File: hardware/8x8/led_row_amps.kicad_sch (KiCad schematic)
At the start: 10 parts

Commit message: Updated Pin Headers
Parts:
- renumbered Row_Amp_1 to Amp_1, Row_Amp_2 to Amp_2
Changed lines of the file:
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@@
   (symbol (lib_id "power:+5V") (at 220.98 95.25 0) (unit 1)
     (in_bom yes) (on_board yes)
-    (property "Reference" "#PWR04" (id 0) (at 220.98 99.06 0)
+    (property "Reference" "#PWR0103" (id 0) (at 220.98 99.06 0)
       (effects (font (size 1.27 1.27)) hide)
     )
@@
   (symbol (lib_id "power:+9V") (at 93.98 64.77 0) (unit 1)
     (in_bom yes) (on_board yes)
-    (property "Reference" "#PWR01" (id 0) (at 93.98 68.58 0)
+    (property "Reference" "#PWR0101" (id 0) (at 93.98 68.58 0)
       (effects (font (size 1.27 1.27)) hide)
     )
@@
   (symbol (lib_id "power:+5V") (at 93.98 95.25 0) (unit 1)
     (in_bom yes) (on_board yes)
-    (property "Reference" "#PWR02" (id 0) (at 93.98 99.06 0)
+    (property "Reference" "#PWR0102" (id 0) (at 93.98 99.06 0)
       (effects (font (size 1.27 1.27)) hide)
     )
@@
   (symbol (lib_id "Op-Amp:MCP619-I{brace}slash}SL") (at 76.2 81.28 0) (unit 1)
     (in_bom yes) (on_board yes) (fields_autoplaced)
-    (property "Reference" "Row_Amp_1" (id 0) (at 76.2 60.96 0))
+    (property "Reference" "Amp_1" (id 0) (at 76.2 60.96 0))
     (property "Value" "MCP619-I{slash}SL" (id 1) (at 76.2 60.96 0)
       (effects (font (size 1.27 1.27)) hide)
@@
   (symbol (lib_id "Op-Amp:MCP619-I{brace}slash}SL") (at 203.2 81.28 0) (unit 1)
     (in_bom yes) (on_board yes) (fields_autoplaced)
-    (property "Reference" "Row_Amp_2" (id 0) (at 203.2 60.96 0))
+    (property "Reference" "Amp_2" (id 0) (at 203.2 60.96 0))
     (property "Value" "MCP619-I{slash}SL" (id 1) (at 203.2 60.96 0)
       (effects (font (size 1.27 1.27)) hide)
@@
   (symbol (lib_id "power:+9V") (at 220.98 64.77 0) (unit 1)
     (in_bom yes) (on_board yes)
-    (property "Reference" "#PWR03" (id 0) (at 220.98 68.58 0)
+    (property "Reference" "#PWR0104" (id 0) (at 220.98 68.58 0)
       (effects (font (size 1.27 1.27)) hide)
     )

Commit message: Temporary Component Placement on PCB
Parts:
- renumbered Amp_1 to AMP_1, Amp_2 to AMP_2
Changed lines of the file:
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@@
   (symbol (lib_id "Op-Amp:MCP619-I{brace}slash}SL") (at 76.2 81.28 0) (unit 1)
     (in_bom yes) (on_board yes) (fields_autoplaced)
-    (property "Reference" "Amp_1" (id 0) (at 76.2 60.96 0))
+    (property "Reference" "AMP_1" (id 0) (at 76.2 60.96 0))
     (property "Value" "MCP619-I{slash}SL" (id 1) (at 76.2 60.96 0)
       (effects (font (size 1.27 1.27)) hide)
@@
   (symbol (lib_id "Op-Amp:MCP619-I{brace}slash}SL") (at 203.2 81.28 0) (unit 1)
     (in_bom yes) (on_board yes) (fields_autoplaced)
-    (property "Reference" "Amp_2" (id 0) (at 203.2 60.96 0))
+    (property "Reference" "AMP_2" (id 0) (at 203.2 60.96 0))
     (property "Value" "MCP619-I{slash}SL" (id 1) (at 203.2 60.96 0)
       (effects (font (size 1.27 1.27)) hide)

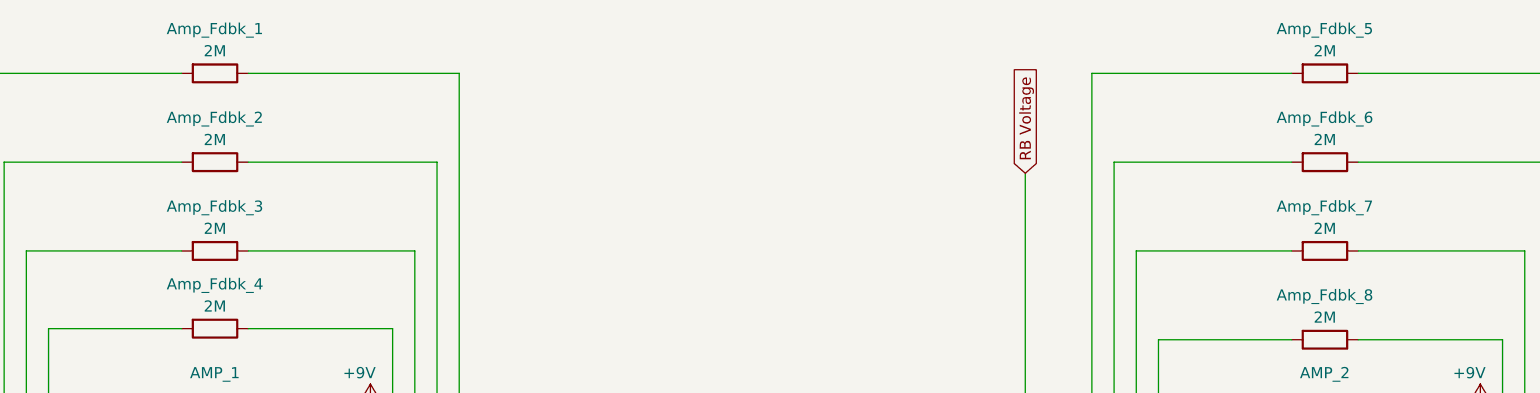
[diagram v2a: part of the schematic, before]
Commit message: Rearranged PCB Components
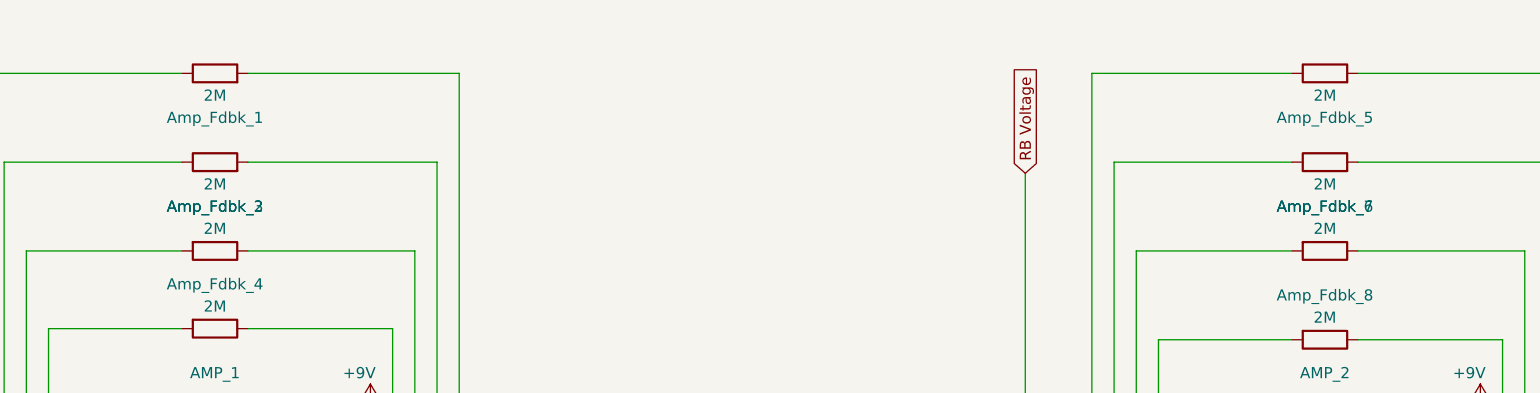
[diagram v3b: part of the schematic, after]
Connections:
- net Amp_IP_1: now also Amp_Fdbk_1.1; no longer Amp_Fdbk_1.2
- net Amp_IP_2: now also Amp_Fdbk_2.1; no longer Amp_Fdbk_2.2
- net Amp_IP_5: now also Amp_Fdbk_5.1; no longer Amp_Fdbk_5.2
- net Amp_IP_6: now also Amp_Fdbk_6.1; no longer Amp_Fdbk_6.2
- net Amp_OP_1: now also Amp_Fdbk_1.2; no longer Amp_Fdbk_1.1
- net Amp_OP_2: now also Amp_Fdbk_2.2; no longer Amp_Fdbk_2.1
- net Amp_OP_5: now also Amp_Fdbk_5.2; no longer Amp_Fdbk_5.1
- net Amp_OP_6: now also Amp_Fdbk_6.2; no longer Amp_Fdbk_6.1
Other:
- moved on the sheet: Amp_Fdbk_1, Amp_Fdbk_2, Amp_Fdbk_5, Amp_Fdbk_6
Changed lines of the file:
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@@
     (effects (font (size 1.27 1.27)) (justify left))
   )
-  (symbol (lib_id "Device:R") (at 76.2 36.83 270) (unit 1)
+  (symbol (lib_id "Device:R") (at 76.2 36.83 90) (unit 1)
     (in_bom yes) (on_board yes)
-    (property "Reference" "Amp_Fdbk_2" (id 0) (at 76.2 31.75 90))
-    (property "Value" "2M" (id 1) (at 76.2 34.29 90))
-    (property "Footprint" "Resistor_THT:R_Axial_DIN0207_L6.3mm_D2.5mm_P7.62mm_Horizontal" (id 2) (at 76.2 35.052 90)
+    (property "Reference" "Amp_Fdbk_2" (id 0) (at 76.2 41.91 90))
+    (property "Value" "2M" (id 1) (at 76.2 39.37 90))
+    (property "Footprint" "Resistor_THT:R_Axial_DIN0207_L6.3mm_D2.5mm_P7.62mm_Horizontal" (id 2) (at 76.2 38.608 90)
       (effects (font (size 1.27 1.27)) hide)
     )
@@
     (pin "2")
   )
-  (symbol (lib_id "Device:R") (at 203.2 36.83 270) (unit 1)
+  (symbol (lib_id "Device:R") (at 203.2 36.83 90) (unit 1)
     (in_bom yes) (on_board yes)
-    (property "Reference" "Amp_Fdbk_6" (id 0) (at 203.2 31.75 90))
-    (property "Value" "2M" (id 1) (at 203.2 34.29 90))
-    (property "Footprint" "Resistor_THT:R_Axial_DIN0207_L6.3mm_D2.5mm_P7.62mm_Horizontal" (id 2) (at 203.2 35.052 90)
+    (property "Reference" "Amp_Fdbk_6" (id 0) (at 203.2 41.91 90))
+    (property "Value" "2M" (id 1) (at 203.2 39.37 90))
+    (property "Footprint" "Resistor_THT:R_Axial_DIN0207_L6.3mm_D2.5mm_P7.62mm_Horizontal" (id 2) (at 203.2 38.608 90)
       (effects (font (size 1.27 1.27)) hide)
     )
@@
     (pin "1")
   )
-  (symbol (lib_id "Device:R") (at 203.2 26.67 270) (unit 1)
+  (symbol (lib_id "Device:R") (at 203.2 26.67 90) (unit 1)
     (in_bom yes) (on_board yes)
-    (property "Reference" "Amp_Fdbk_5" (id 0) (at 203.2 21.59 90))
-    (property "Value" "2M" (id 1) (at 203.2 24.13 90))
-    (property "Footprint" "Resistor_THT:R_Axial_DIN0207_L6.3mm_D2.5mm_P7.62mm_Horizontal" (id 2) (at 203.2 24.892 90)
+    (property "Reference" "Amp_Fdbk_5" (id 0) (at 203.2 31.75 90))
+    (property "Value" "2M" (id 1) (at 203.2 29.21 90))
+    (property "Footprint" "Resistor_THT:R_Axial_DIN0207_L6.3mm_D2.5mm_P7.62mm_Horizontal" (id 2) (at 203.2 28.448 90)
       (effects (font (size 1.27 1.27)) hide)
     )
@@
     (pin "2")
   )
-  (symbol (lib_id "Device:R") (at 76.2 26.67 270) (unit 1)
+  (symbol (lib_id "Device:R") (at 76.2 26.67 90) (unit 1)
     (in_bom yes) (on_board yes)
-    (property "Reference" "Amp_Fdbk_1" (id 0) (at 76.2 21.59 90))
-    (property "Value" "2M" (id 1) (at 76.2 24.13 90))
-    (property "Footprint" "Resistor_THT:R_Axial_DIN0207_L6.3mm_D2.5mm_P7.62mm_Horizontal" (id 2) (at 76.2 24.892 90)
+    (property "Reference" "Amp_Fdbk_1" (id 0) (at 76.2 31.75 90))
+    (property "Value" "2M" (id 1) (at 76.2 29.21 90))
+    (property "Footprint" "Resistor_THT:R_Axial_DIN0207_L6.3mm_D2.5mm_P7.62mm_Horizontal" (id 2) (at 76.2 28.448 90)
       (effects (font (size 1.27 1.27)) hide)
     )

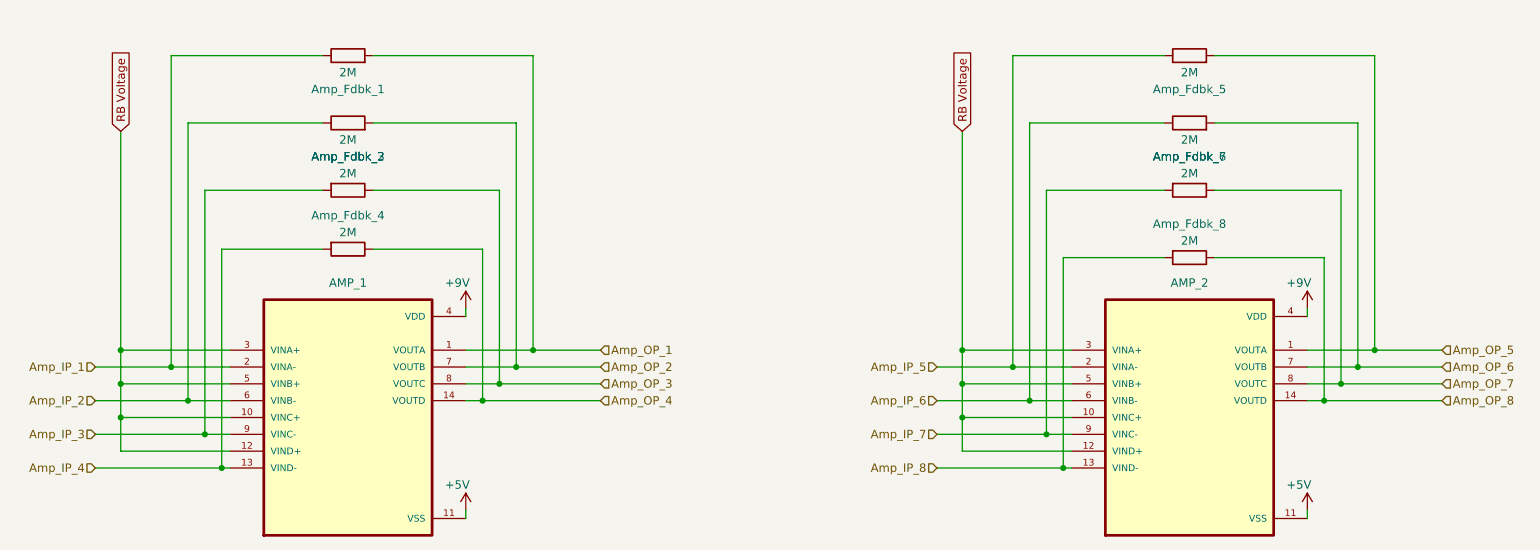
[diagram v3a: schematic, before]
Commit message: Updated Footprints
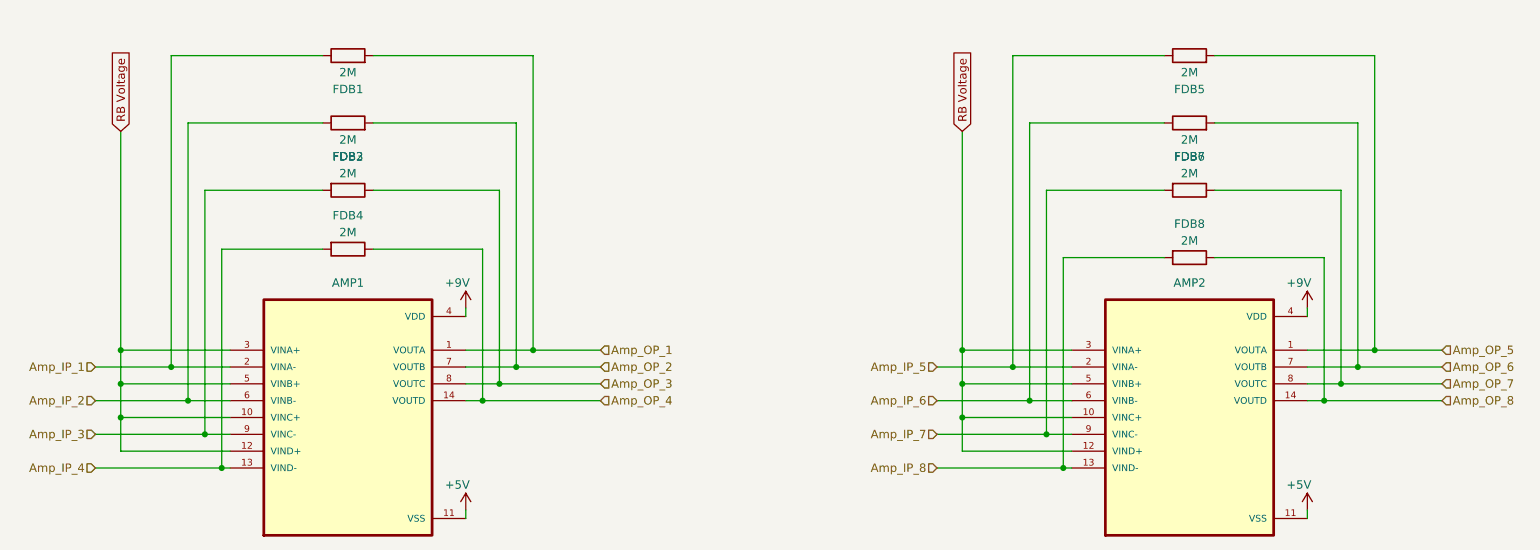
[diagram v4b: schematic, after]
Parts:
- FDB1: renamed from Amp_Fdbk_1; footprint Resistor_THT:R_Axial_DIN0207_L6.3mm_D2.5mm_P7.62mm_Horizontal -> Resistor TH:footprints
- FDB2: renamed from Amp_Fdbk_2; footprint Resistor_THT:R_Axial_DIN0207_L6.3mm_D2.5mm_P7.62mm_Horizontal -> Resistor TH:footprints
- FDB3: renamed from Amp_Fdbk_3; footprint Resistor_THT:R_Axial_DIN0207_L6.3mm_D2.5mm_P7.62mm_Horizontal -> Resistor TH:footprints
- FDB4: renamed from Amp_Fdbk_4; footprint Resistor_THT:R_Axial_DIN0207_L6.3mm_D2.5mm_P7.62mm_Horizontal -> Resistor TH:footprints
- FDB5: renamed from Amp_Fdbk_5; footprint Resistor_THT:R_Axial_DIN0207_L6.3mm_D2.5mm_P7.62mm_Horizontal -> Resistor TH:footprints
- FDB6: renamed from Amp_Fdbk_6; footprint Resistor_THT:R_Axial_DIN0207_L6.3mm_D2.5mm_P7.62mm_Horizontal -> Resistor TH:footprints
- FDB7: renamed from Amp_Fdbk_7; footprint Resistor_THT:R_Axial_DIN0207_L6.3mm_D2.5mm_P7.62mm_Horizontal -> Resistor TH:footprints
- FDB8: renamed from Amp_Fdbk_8; footprint Resistor_THT:R_Axial_DIN0207_L6.3mm_D2.5mm_P7.62mm_Horizontal -> Resistor TH:footprints
- renumbered AMP_1 to AMP1, AMP_2 to AMP2
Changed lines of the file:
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@@
   (symbol (lib_id "Device:R") (at 76.2 36.83 90) (unit 1)
     (in_bom yes) (on_board yes)
-    (property "Reference" "Amp_Fdbk_2" (id 0) (at 76.2 41.91 90))
+    (property "Reference" "FDB2" (id 0) (at 76.2 41.91 90))
     (property "Value" "2M" (id 1) (at 76.2 39.37 90))
-    (property "Footprint" "Resistor_THT:R_Axial_DIN0207_L6.3mm_D2.5mm_P7.62mm_Horizontal" (id 2) (at 76.2 38.608 90)
+    (property "Footprint" "Resistor TH:footprints" (id 2) (at 76.2 38.608 90)
       (effects (font (size 1.27 1.27)) hide)
     )
@@
   (symbol (lib_id "Device:R") (at 203.2 46.99 270) (unit 1)
     (in_bom yes) (on_board yes)
-    (property "Reference" "Amp_Fdbk_7" (id 0) (at 203.2 41.91 90))
+    (property "Reference" "FDB7" (id 0) (at 203.2 41.91 90))
     (property "Value" "2M" (id 1) (at 203.2 44.45 90))
-    (property "Footprint" "Resistor_THT:R_Axial_DIN0207_L6.3mm_D2.5mm_P7.62mm_Horizontal" (id 2) (at 203.2 45.212 90)
+    (property "Footprint" "Resistor TH:footprints" (id 2) (at 203.2 45.212 90)
       (effects (font (size 1.27 1.27)) hide)
     )
@@
   (symbol (lib_id "Device:R") (at 203.2 36.83 90) (unit 1)
     (in_bom yes) (on_board yes)
-    (property "Reference" "Amp_Fdbk_6" (id 0) (at 203.2 41.91 90))
+    (property "Reference" "FDB6" (id 0) (at 203.2 41.91 90))
     (property "Value" "2M" (id 1) (at 203.2 39.37 90))
-    (property "Footprint" "Resistor_THT:R_Axial_DIN0207_L6.3mm_D2.5mm_P7.62mm_Horizontal" (id 2) (at 203.2 38.608 90)
+    (property "Footprint" "Resistor TH:footprints" (id 2) (at 203.2 38.608 90)
       (effects (font (size 1.27 1.27)) hide)
     )
@@
   (symbol (lib_id "Device:R") (at 203.2 26.67 90) (unit 1)
     (in_bom yes) (on_board yes)
-    (property "Reference" "Amp_Fdbk_5" (id 0) (at 203.2 31.75 90))
+    (property "Reference" "FDB5" (id 0) (at 203.2 31.75 90))
     (property "Value" "2M" (id 1) (at 203.2 29.21 90))
-    (property "Footprint" "Resistor_THT:R_Axial_DIN0207_L6.3mm_D2.5mm_P7.62mm_Horizontal" (id 2) (at 203.2 28.448 90)
+    (property "Footprint" "Resistor TH:footprints" (id 2) (at 203.2 28.448 90)
       (effects (font (size 1.27 1.27)) hide)
     )
@@
   (symbol (lib_id "Device:R") (at 76.2 26.67 90) (unit 1)
     (in_bom yes) (on_board yes)
-    (property "Reference" "Amp_Fdbk_1" (id 0) (at 76.2 31.75 90))
+    (property "Reference" "FDB1" (id 0) (at 76.2 31.75 90))
     (property "Value" "2M" (id 1) (at 76.2 29.21 90))
-    (property "Footprint" "Resistor_THT:R_Axial_DIN0207_L6.3mm_D2.5mm_P7.62mm_Horizontal" (id 2) (at 76.2 28.448 90)
+    (property "Footprint" "Resistor TH:footprints" (id 2) (at 76.2 28.448 90)
       (effects (font (size 1.27 1.27)) hide)
     )
@@
   (symbol (lib_id "Op-Amp:MCP619-I{brace}slash}SL") (at 76.2 81.28 0) (unit 1)
     (in_bom yes) (on_board yes) (fields_autoplaced)
-    (property "Reference" "AMP_1" (id 0) (at 76.2 60.96 0))
+    (property "Reference" "AMP1" (id 0) (at 76.2 60.96 0))
     (property "Value" "MCP619-I{slash}SL" (id 1) (at 76.2 60.96 0)
       (effects (font (size 1.27 1.27)) hide)
@@
   (symbol (lib_id "Device:R") (at 76.2 55.88 270) (unit 1)
     (in_bom yes) (on_board yes)
-    (property "Reference" "Amp_Fdbk_4" (id 0) (at 76.2 50.8 90))
+    (property "Reference" "FDB4" (id 0) (at 76.2 50.8 90))
     (property "Value" "2M" (id 1) (at 76.2 53.34 90))
-    (property "Footprint" "Resistor_THT:R_Axial_DIN0207_L6.3mm_D2.5mm_P7.62mm_Horizontal" (id 2) (at 76.2 54.102 90)
+    (property "Footprint" "Resistor TH:footprints" (id 2) (at 76.2 54.102 90)
       (effects (font (size 1.27 1.27)) hide)
     )
@@
   (symbol (lib_id "Op-Amp:MCP619-I{brace}slash}SL") (at 203.2 81.28 0) (unit 1)
     (in_bom yes) (on_board yes) (fields_autoplaced)
-    (property "Reference" "AMP_2" (id 0) (at 203.2 60.96 0))
+    (property "Reference" "AMP2" (id 0) (at 203.2 60.96 0))
     (property "Value" "MCP619-I{slash}SL" (id 1) (at 203.2 60.96 0)
       (effects (font (size 1.27 1.27)) hide)
@@
   (symbol (lib_id "Device:R") (at 203.2 57.15 270) (unit 1)
     (in_bom yes) (on_board yes)
-    (property "Reference" "Amp_Fdbk_8" (id 0) (at 203.2 52.07 90))
+    (property "Reference" "FDB8" (id 0) (at 203.2 52.07 90))
     (property "Value" "2M" (id 1) (at 203.2 54.61 90))
-    (property "Footprint" "Resistor_THT:R_Axial_DIN0207_L6.3mm_D2.5mm_P7.62mm_Horizontal" (id 2) (at 203.2 55.372 90)
+    (property "Footprint" "Resistor TH:footprints" (id 2) (at 203.2 55.372 90)
       (effects (font (size 1.27 1.27)) hide)
     )
@@
   (symbol (lib_id "Device:R") (at 76.2 46.99 270) (unit 1)
     (in_bom yes) (on_board yes)
-    (property "Reference" "Amp_Fdbk_3" (id 0) (at 76.2 41.91 90))
+    (property "Reference" "FDB3" (id 0) (at 76.2 41.91 90))
     (property "Value" "2M" (id 1) (at 76.2 44.45 90))
-    (property "Footprint" "Resistor_THT:R_Axial_DIN0207_L6.3mm_D2.5mm_P7.62mm_Horizontal" (id 2) (at 76.2 45.212 90)
-      (effects (font (size 1.27 1.27)) hide)
-    )
+    (property "Footprint" "Resistor TH:footprints" (id 2) (at 76.2 45.212 90)
+      (effects (font (size 1.27 1.27)) hide)
+    )

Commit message: Completed Major Routing
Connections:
- net Amp_IP_1: now also FDB1.2; no longer FDB1.1
- net Amp_IP_2: now also FDB2.2; no longer FDB2.1
- net Amp_IP_5: now also FDB5.2; no longer FDB5.1
- net Amp_IP_6: now also FDB6.2; no longer FDB6.1
- net Amp_OP_1: now also FDB1.1; no longer FDB1.2
- net Amp_OP_2: now also FDB2.1; no longer FDB2.2
- net Amp_OP_5: now also FDB5.1; no longer FDB5.2
- net Amp_OP_6: now also FDB6.1; no longer FDB6.2
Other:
- moved on the sheet: FDB1, FDB2, FDB5, FDB6
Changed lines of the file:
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@@
     (effects (font (size 1.27 1.27)) (justify left))
   )
-  (symbol (lib_id "Device:R") (at 76.2 36.83 90) (unit 1)
+  (symbol (lib_id "Device:R") (at 76.2 36.83 270) (unit 1)
     (in_bom yes) (on_board yes)
-    (property "Reference" "FDB2" (id 0) (at 76.2 41.91 90))
-    (property "Value" "2M" (id 1) (at 76.2 39.37 90))
-    (property "Footprint" "Resistor TH:footprints" (id 2) (at 76.2 38.608 90)
+    (property "Reference" "FDB2" (id 0) (at 76.2 31.75 90))
+    (property "Value" "2M" (id 1) (at 76.2 34.29 90))
+    (property "Footprint" "Resistor TH:footprints" (id 2) (at 76.2 35.052 90)
       (effects (font (size 1.27 1.27)) hide)
     )
@@
     (pin "2")
   )
-  (symbol (lib_id "Device:R") (at 203.2 36.83 90) (unit 1)
+  (symbol (lib_id "Device:R") (at 203.2 36.83 270) (unit 1)
     (in_bom yes) (on_board yes)
-    (property "Reference" "FDB6" (id 0) (at 203.2 41.91 90))
-    (property "Value" "2M" (id 1) (at 203.2 39.37 90))
-    (property "Footprint" "Resistor TH:footprints" (id 2) (at 203.2 38.608 90)
+    (property "Reference" "FDB6" (id 0) (at 203.2 31.75 90))
+    (property "Value" "2M" (id 1) (at 203.2 34.29 90))
+    (property "Footprint" "Resistor TH:footprints" (id 2) (at 203.2 35.052 90)
       (effects (font (size 1.27 1.27)) hide)
     )
@@
   (symbol (lib_id "power:+5V") (at 220.98 95.25 0) (unit 1)
     (in_bom yes) (on_board yes)
-    (property "Reference" "#PWR0103" (id 0) (at 220.98 99.06 0)
+    (property "Reference" "#PWR0101" (id 0) (at 220.98 99.06 0)
       (effects (font (size 1.27 1.27)) hide)
     )
@@
   (symbol (lib_id "power:+9V") (at 93.98 64.77 0) (unit 1)
     (in_bom yes) (on_board yes)
-    (property "Reference" "#PWR0101" (id 0) (at 93.98 68.58 0)
+    (property "Reference" "#PWR0103" (id 0) (at 93.98 68.58 0)
       (effects (font (size 1.27 1.27)) hide)
     )
@@
     (pin "1")
   )
-  (symbol (lib_id "Device:R") (at 203.2 26.67 90) (unit 1)
+  (symbol (lib_id "Device:R") (at 203.2 26.67 270) (unit 1)
     (in_bom yes) (on_board yes)
-    (property "Reference" "FDB5" (id 0) (at 203.2 31.75 90))
-    (property "Value" "2M" (id 1) (at 203.2 29.21 90))
-    (property "Footprint" "Resistor TH:footprints" (id 2) (at 203.2 28.448 90)
+    (property "Reference" "FDB5" (id 0) (at 203.2 21.59 90))
+    (property "Value" "2M" (id 1) (at 203.2 24.13 90))
+    (property "Footprint" "Resistor TH:footprints" (id 2) (at 203.2 24.892 90)
       (effects (font (size 1.27 1.27)) hide)
     )
@@
     (pin "2")
   )
-  (symbol (lib_id "Device:R") (at 76.2 26.67 90) (unit 1)
+  (symbol (lib_id "Device:R") (at 76.2 26.67 270) (unit 1)
     (in_bom yes) (on_board yes)
-    (property "Reference" "FDB1" (id 0) (at 76.2 31.75 90))
-    (property "Value" "2M" (id 1) (at 76.2 29.21 90))
-    (property "Footprint" "Resistor TH:footprints" (id 2) (at 76.2 28.448 90)
+    (property "Reference" "FDB1" (id 0) (at 76.2 21.59 90))
+    (property "Value" "2M" (id 1) (at 76.2 24.13 90))
+    (property "Footprint" "Resistor TH:footprints" (id 2) (at 76.2 24.892 90)
       (effects (font (size 1.27 1.27)) hide)
     )
@@
   (symbol (lib_id "power:+5V") (at 93.98 95.25 0) (unit 1)
     (in_bom yes) (on_board yes)
-    (property "Reference" "#PWR0102" (id 0) (at 93.98 99.06 0)
+    (property "Reference" "#PWR0104" (id 0) (at 93.98 99.06 0)
       (effects (font (size 1.27 1.27)) hide)
     )
@@
   (symbol (lib_id "power:+9V") (at 220.98 64.77 0) (unit 1)
     (in_bom yes) (on_board yes)
-    (property "Reference" "#PWR0104" (id 0) (at 220.98 68.58 0)
+    (property "Reference" "#PWR0102" (id 0) (at 220.98 68.58 0)
       (effects (font (size 1.27 1.27)) hide)
     )
